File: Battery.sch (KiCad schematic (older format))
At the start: 21 parts, among them J3 USB_C_Receptacle_USB2.0, U4 SY6926

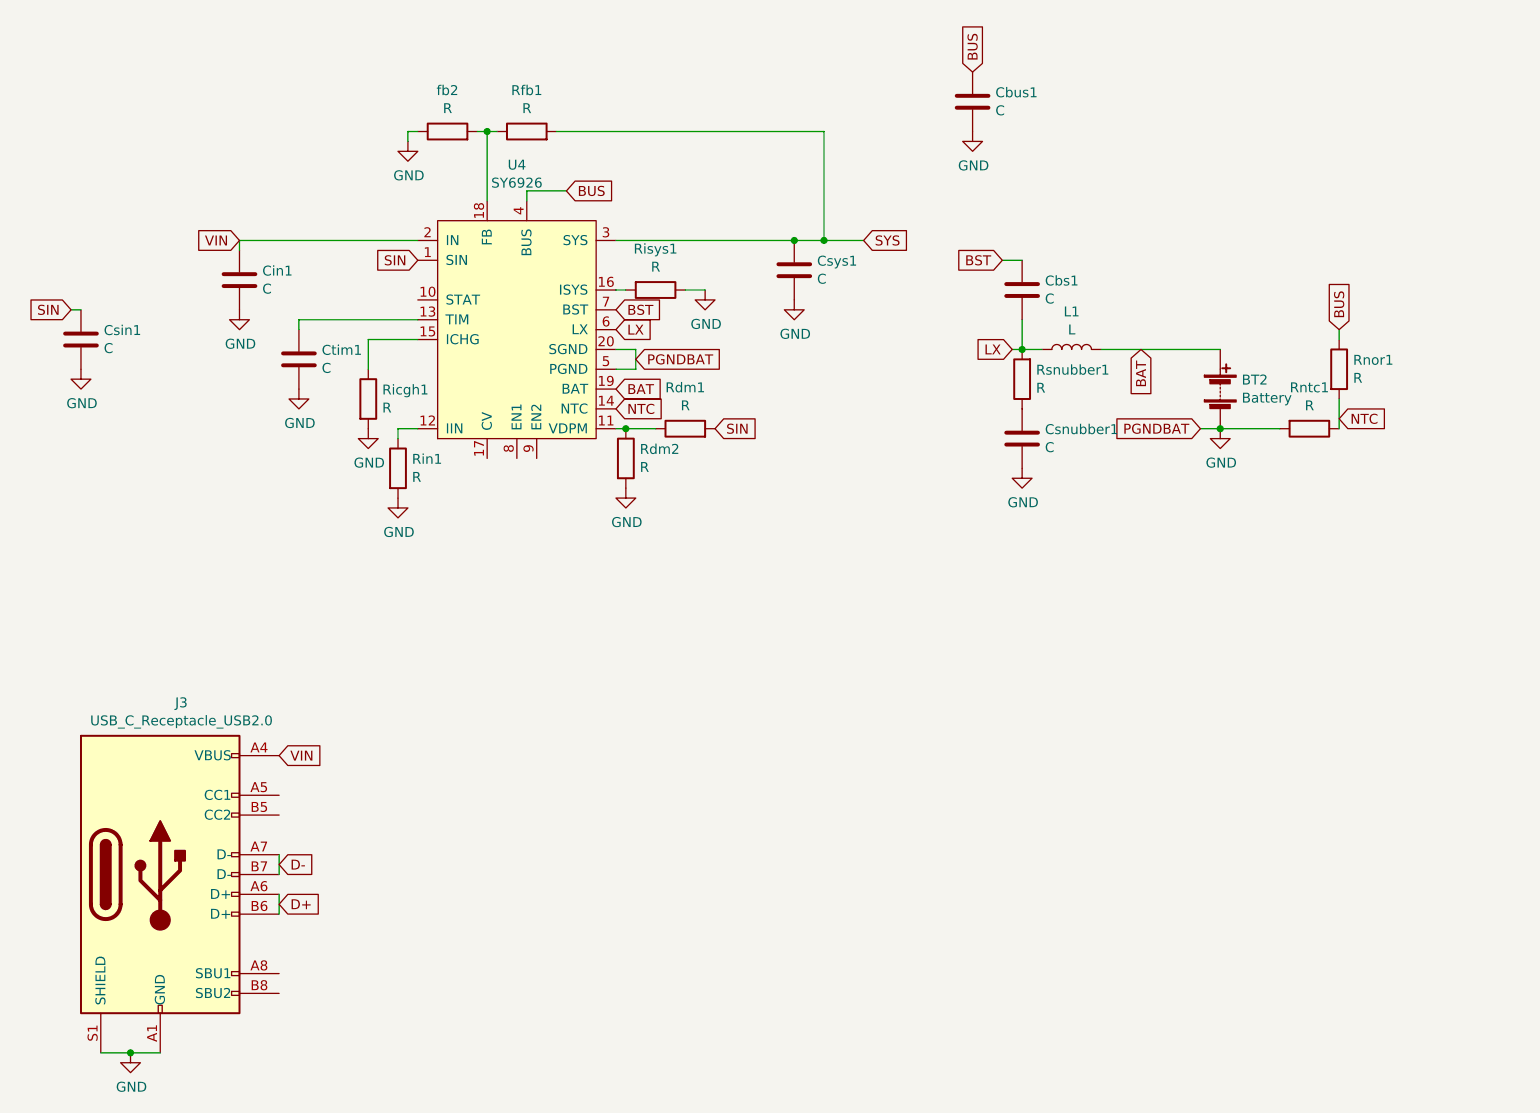
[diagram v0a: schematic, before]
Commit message: Added hardware battery disconnect
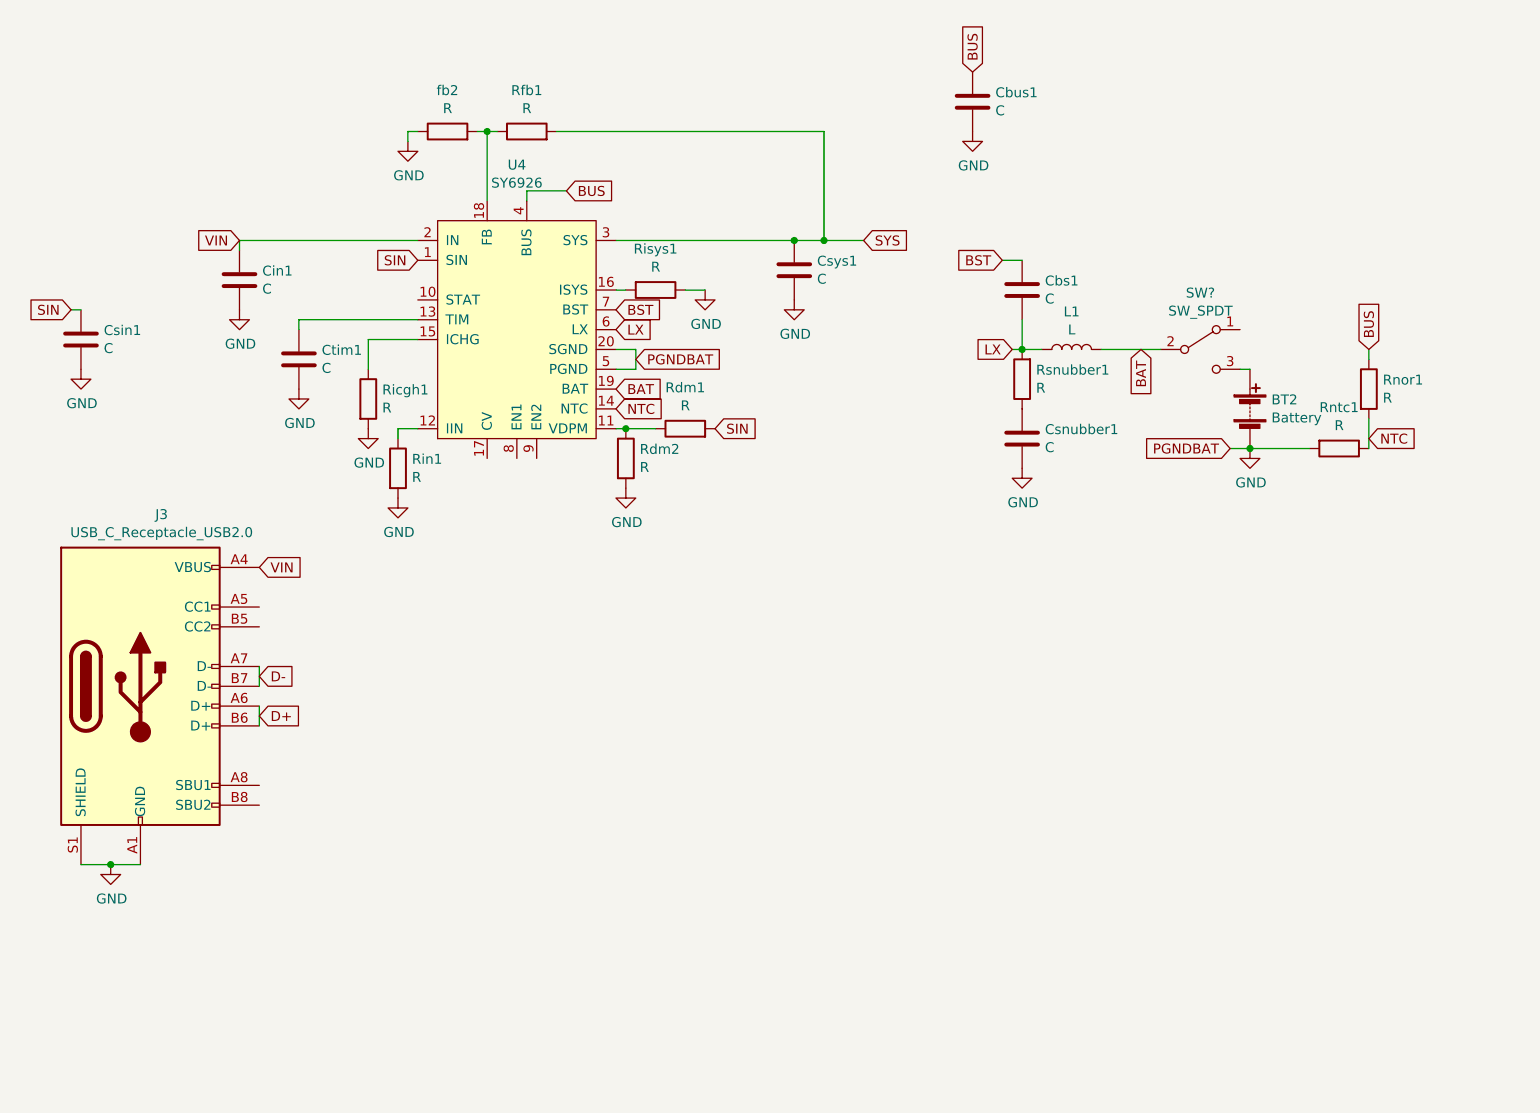
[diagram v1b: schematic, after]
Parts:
- added SW?: SW_SPDT, Hardware:SWINTCHFORBATTERY, symbol Switch:SW_SPDT
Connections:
- net BAT: now also SW?.2 (B); no longer BT2.1 (+)
- new net: BT2.1 (+), SW?.3 (C)
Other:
- moved on the sheet: BT2, J3, Rnor1, Rntc1
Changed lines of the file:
@@
 L Device:Battery BT2
 U 1 1 60BFF57C
-P 6650 2900
-F 0 "BT2" H 6758 2946 50  0000 L CNN
-F 1 "Battery" H 6758 2855 50  0000 L CNN
-F 2 "Connector_PinHeader_2.54mm:PinHeader_1x02_P2.54mm_Vertical" V 6650 2960 50  0001 C CNN
-F 3 "~" V 6650 2960 50  0001 C CNN
-	1    6650 2900
+P 6800 3000
+F 0 "BT2" H 6908 3046 50  0000 L CNN
+F 1 "Battery" H 6908 2955 50  0000 L CNN
+F 2 "Connector_PinHeader_2.54mm:PinHeader_1x02_P2.54mm_Vertical" V 6800 3060 50  0001 C CNN
+F 3 "~" V 6800 3060 50  0001 C CNN
+	1    6800 3000
 	1    0    0    -1
 $EndComp
@@
 $EndComp
 Wire Wire Line
-	6550 3100 6650 3100
+	6700 3200 6800 3200
 $Comp
 L power:GND #PWR028
 U 1 1 60C0B9D9
-P 6650 3100
-F 0 "#PWR028" H 6650 2850 50  0001 C CNN
-F 1 "GND" H 6655 2927 50  0000 C CNN
-F 2 "" H 6650 3100 50  0001 C CNN
-F 3 "" H 6650 3100 50  0001 C CNN
-	1    6650 3100
-	1    0    0    -1
-$EndComp
-Connection ~ 6650 3100
+P 6800 3200
+F 0 "#PWR028" H 6800 2950 50  0001 C CNN
+F 1 "GND" H 6805 3027 50  0000 C CNN
+F 2 "" H 6800 3200 50  0001 C CNN
+F 3 "" H 6800 3200 50  0001 C CNN
+	1    6800 3200
+	1    0    0    -1
+$EndComp
+Connection ~ 6800 3200
 Text GLabel 3350 1900 2    50   Input ~ 0
 BUS
-Text GLabel 7250 2600 1    50   Input ~ 0
+Text GLabel 7400 2700 1    50   Input ~ 0
 BUS
 $Comp
 L Device:R Rnor1
 U 1 1 60C0CFEE
-P 7250 2800
-F 0 "Rnor1" H 7320 2846 50  0000 L CNN
-F 1 "R" H 7320 2755 50  0000 L CNN
-F 2 "Resistor_SMD:R_0805_2012Metric" V 7180 2800 50  0001 C CNN
-F 3 "~" H 7250 2800 50  0001 C CNN
-	1    7250 2800
+P 7400 2900
+F 0 "Rnor1" H 7470 2946 50  0000 L CNN
+F 1 "R" H 7470 2855 50  0000 L CNN
+F 2 "Resistor_SMD:R_0805_2012Metric" V 7330 2900 50  0001 C CNN
+F 3 "~" H 7400 2900 50  0001 C CNN
+	1    7400 2900
 	1    0    0    -1
 $EndComp
@@
 L Device:R Rntc1
 U 1 1 60C0D8A7
-P 7100 3100
-F 0 "Rntc1" V 6893 3100 50  0000 C CNN
-F 1 "R" V 6984 3100 50  0000 C CNN
-F 2 "Resistor_SMD:R_0805_2012Metric" V 7030 3100 50  0001 C CNN
-F 3 "~" H 7100 3100 50  0001 C CNN
-	1    7100 3100
+P 7250 3200
+F 0 "Rntc1" V 7043 3200 50  0000 C CNN
+F 1 "R" V 7134 3200 50  0000 C CNN
+F 2 "Resistor_SMD:R_0805_2012Metric" V 7180 3200 50  0001 C CNN
+F 3 "~" H 7250 3200 50  0001 C CNN
+	1    7250 3200
 	0    1    1    0
 $EndComp
 Wire Wire Line
-	7250 3100 7250 2950
-Wire Wire Line
-	7250 2650 7250 2600
+	7400 3200 7400 3050
+Wire Wire Line
+	7400 2750 7400 2700
 $Comp
 L Device:L L1
@@
 Text GLabel 3700 2750 2    50   Input ~ 0
 PGNDBAT
-Wire Wire Line
-	6050 2700 6650 2700
 Text GLabel 3600 2500 2    50   Input ~ 0
 BST
@@
 Text GLabel 5600 2700 0    50   Input ~ 0
 LX
-Text GLabel 6550 3100 0    50   Input ~ 0
+Text GLabel 6700 3200 0    50   Input ~ 0
 PGNDBAT
 Wire Wire Line
@@
 Text GLabel 3600 3000 2    50   Input ~ 0
 NTC
-Text GLabel 7250 3050 2    50   Input ~ 0
+Text GLabel 7400 3150 2    50   Input ~ 0
 NTC
 Wire Wire Line
@@
 $EndComp
 Wire Wire Line
-	6650 3100 6950 3100
+	6800 3200 7100 3200
 Wire Wire Line
 	3350 1900 3150 1900
@@
 L Connector:USB_C_Receptacle_USB2.0 J3
 U 1 1 610152FB
-P 1300 5350
-F 0 "J3" H 1407 6217 50  0000 C CNN
-F 1 "USB_C_Receptacle_USB2.0" H 1407 6126 50  0000 C CNN
-F 2 "Connector_USB:USB_C_Receptacle_XKB_U262-16XN-4BVC11" H 1450 5350 50  0001 C CNN
-F 3 "https://www.usb.org/sites/default/files/documents/usb_type-c.zip" H 1450 5350 50  0001 C CNN
-	1    1300 5350
-	1    0    0    -1
-$EndComp
-Wire Wire Line
-	1300 6250 1150 6250
+P 1200 4400
+F 0 "J3" H 1307 5267 50  0000 C CNN
+F 1 "USB_C_Receptacle_USB2.0" H 1307 5176 50  0000 C CNN
+F 2 "Connector_USB:USB_C_Receptacle_XKB_U262-16XN-4BVC11" H 1350 4400 50  0001 C CNN
+F 3 "https://www.usb.org/sites/default/files/documents/usb_type-c.zip" H 1350 4400 50  0001 C CNN
+	1    1200 4400
+	1    0    0    -1
+$EndComp
+Wire Wire Line
+	1200 5300 1050 5300
 $Comp
 L power:GND #PWR053
 U 1 1 6101E2A9
-P 1150 6250
-F 0 "#PWR053" H 1150 6000 50  0001 C CNN
-F 1 "GND" H 1155 6077 50  0000 C CNN
-F 2 "" H 1150 6250 50  0001 C CNN
-F 3 "" H 1150 6250 50  0001 C CNN
-	1    1150 6250
-	1    0    0    -1
-$EndComp
-Connection ~ 1150 6250
-Wire Wire Line
-	1150 6250 1000 6250
+P 1050 5300
+F 0 "#PWR053" H 1050 5050 50  0001 C CNN
+F 1 "GND" H 1055 5127 50  0000 C CNN
+F 2 "" H 1050 5300 50  0001 C CNN
+F 3 "" H 1050 5300 50  0001 C CNN
+	1    1050 5300
+	1    0    0    -1
+$EndComp
+Connection ~ 1050 5300
+Wire Wire Line
+	1050 5300 900  5300
 Text GLabel 1700 2150 0    50   Input ~ 0
 VIN
-Text GLabel 1900 4750 2    50   Input ~ 0
+Text GLabel 1800 3800 2    50   Input ~ 0
 VIN
 Wire Wire Line
-	1900 5250 1900 5350
-Wire Wire Line
-	1900 5450 1900 5550
-Text GLabel 1900 5300 2    50   Input ~ 0
+	1800 4300 1800 4400
+Wire Wire Line
+	1800 4500 1800 4600
+Text GLabel 1800 4350 2    50   Input ~ 0
 D-
-Text GLabel 1900 5500 2    50   Input ~ 0
+Text GLabel 1800 4550 2    50   Input ~ 0
 D+
+Wire Wire Line
+	6800 2800 6750 2800
+Wire Wire Line
+	6050 2700 6350 2700
+$Comp
+L Switch:SW_SPDT SW?
+U 1 1 60A4FBE3
+P 6550 2700
+F 0 "SW?" H 6550 2985 50  0000 C CNN
+F 1 "SW_SPDT" H 6550 2894 50  0000 C CNN
+F 2 "Hardware:SWINTCHFORBATTERY" H 6550 2700 50  0001 C CNN
+F 3 "~" H 6550 2700 50  0001 C CNN
+	1    6550 2700
+	1    0    0    -1
+$EndComp
 $EndSCHEMATC

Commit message: Ja crap toch weer aan de PCB gezeten
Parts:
- gave numbers to parts that had none: 1
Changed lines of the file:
@@
 	6050 2700 6350 2700
 $Comp
-L Switch:SW_SPDT SW?
+L Switch:SW_SPDT SW2
 U 1 1 60A4FBE3
 P 6550 2700
-F 0 "SW?" H 6550 2985 50  0000 C CNN
+F 0 "SW2" H 6550 2985 50  0000 C CNN
 F 1 "SW_SPDT" H 6550 2894 50  0000 C CNN
 F 2 "Hardware:SWINTCHFORBATTERY" H 6550 2700 50  0001 C CNN

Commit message: Added SY6926 component values and some minor cleanup
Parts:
- Cin1: value C -> 20uF
- L1: value L -> 1.65uH
- Rdm1, Rfb1: value R -> 33K
- Rdm2: value R -> 9.1K
- Ricgh1: value R -> 10.666K
- Rin1: value R -> 1K
- Risys1: value R -> 36K
- fb2: value R -> 10.3K
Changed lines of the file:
@@
 P 3650 3250
 F 0 "Rdm2" H 3720 3296 50  0000 L CNN
-F 1 "R" H 3720 3205 50  0000 L CNN
+F 1 "9.1K" H 3720 3205 50  0000 L CNN
 F 2 "Resistor_SMD:R_0805_2012Metric" V 3580 3250 50  0001 C CNN
 F 3 "~" H 3650 3250 50  0001 C CNN
@@
 P 3950 3100
 F 0 "Rdm1" V 4157 3100 50  0000 C CNN
-F 1 "R" V 4066 3100 50  0000 C CNN
+F 1 "33K" V 4066 3100 50  0000 C CNN
 F 2 "Resistor_SMD:R_0805_2012Metric" V 3880 3100 50  0001 C CNN
 F 3 "~" H 3950 3100 50  0001 C CNN
@@
 P 2500 3300
 F 0 "Rin1" H 2570 3346 50  0000 L CNN
-F 1 "R" H 2570 3255 50  0000 L CNN
+F 1 "1K" H 2570 3255 50  0000 L CNN
 F 2 "Resistor_SMD:R_0805_2012Metric" V 2430 3300 50  0001 C CNN
 F 3 "~" H 2500 3300 50  0001 C CNN
@@
 P 2350 2950
 F 0 "Ricgh1" H 2420 2996 50  0000 L CNN
-F 1 "R" H 2420 2905 50  0000 L CNN
+F 1 "10.666K" H 2420 2905 50  0000 L CNN
 F 2 "Resistor_SMD:R_0805_2012Metric" V 2280 2950 50  0001 C CNN
 F 3 "~" H 2350 2950 50  0001 C CNN
@@
 P 1700 2350
 F 0 "Cin1" H 1815 2396 50  0000 L CNN
-F 1 "C" H 1815 2305 50  0000 L CNN
+F 1 "20uF" H 1815 2305 50  0000 L CNN
 F 2 "Capacitor_SMD:C_0805_2012Metric" H 1738 2200 50  0001 C CNN
 F 3 "~" H 1700 2350 50  0001 C CNN
@@
 P 5900 2700
 F 0 "L1" V 6090 2700 50  0000 C CNN
-F 1 "L" V 5999 2700 50  0000 C CNN
+F 1 "1.65uH" V 5999 2700 50  0000 C CNN
 F 2 "Connector_PinHeader_2.54mm:PinHeader_1x02_P2.54mm_Vertical" H 5900 2700 50  0001 C CNN
 F 3 "~" H 5900 2700 50  0001 C CNN
@@
 P 3800 2400
 F 0 "Risys1" V 3593 2400 50  0000 C CNN
-F 1 "R" V 3684 2400 50  0000 C CNN
+F 1 "36K" V 3684 2400 50  0000 C CNN
 F 2 "Resistor_SMD:R_0805_2012Metric" V 3730 2400 50  0001 C CNN
 F 3 "~" H 3800 2400 50  0001 C CNN
@@
 P 2750 1600
 F 0 "fb2" V 2957 1600 50  0000 C CNN
-F 1 "R" V 2866 1600 50  0000 C CNN
+F 1 "10.3K" V 2866 1600 50  0000 C CNN
 F 2 "Resistor_SMD:R_0805_2012Metric" V 2680 1600 50  0001 C CNN
 F 3 "~" H 2750 1600 50  0001 C CNN
@@
 P 3150 1600
 F 0 "Rfb1" V 3357 1600 50  0000 C CNN
-F 1 "R" V 3266 1600 50  0000 C CNN
+F 1 "33K" V 3266 1600 50  0000 C CNN
 F 2 "Resistor_SMD:R_0805_2012Metric" V 3080 1600 50  0001 C CNN
 F 3 "~" H 3150 1600 50  0001 C CNN

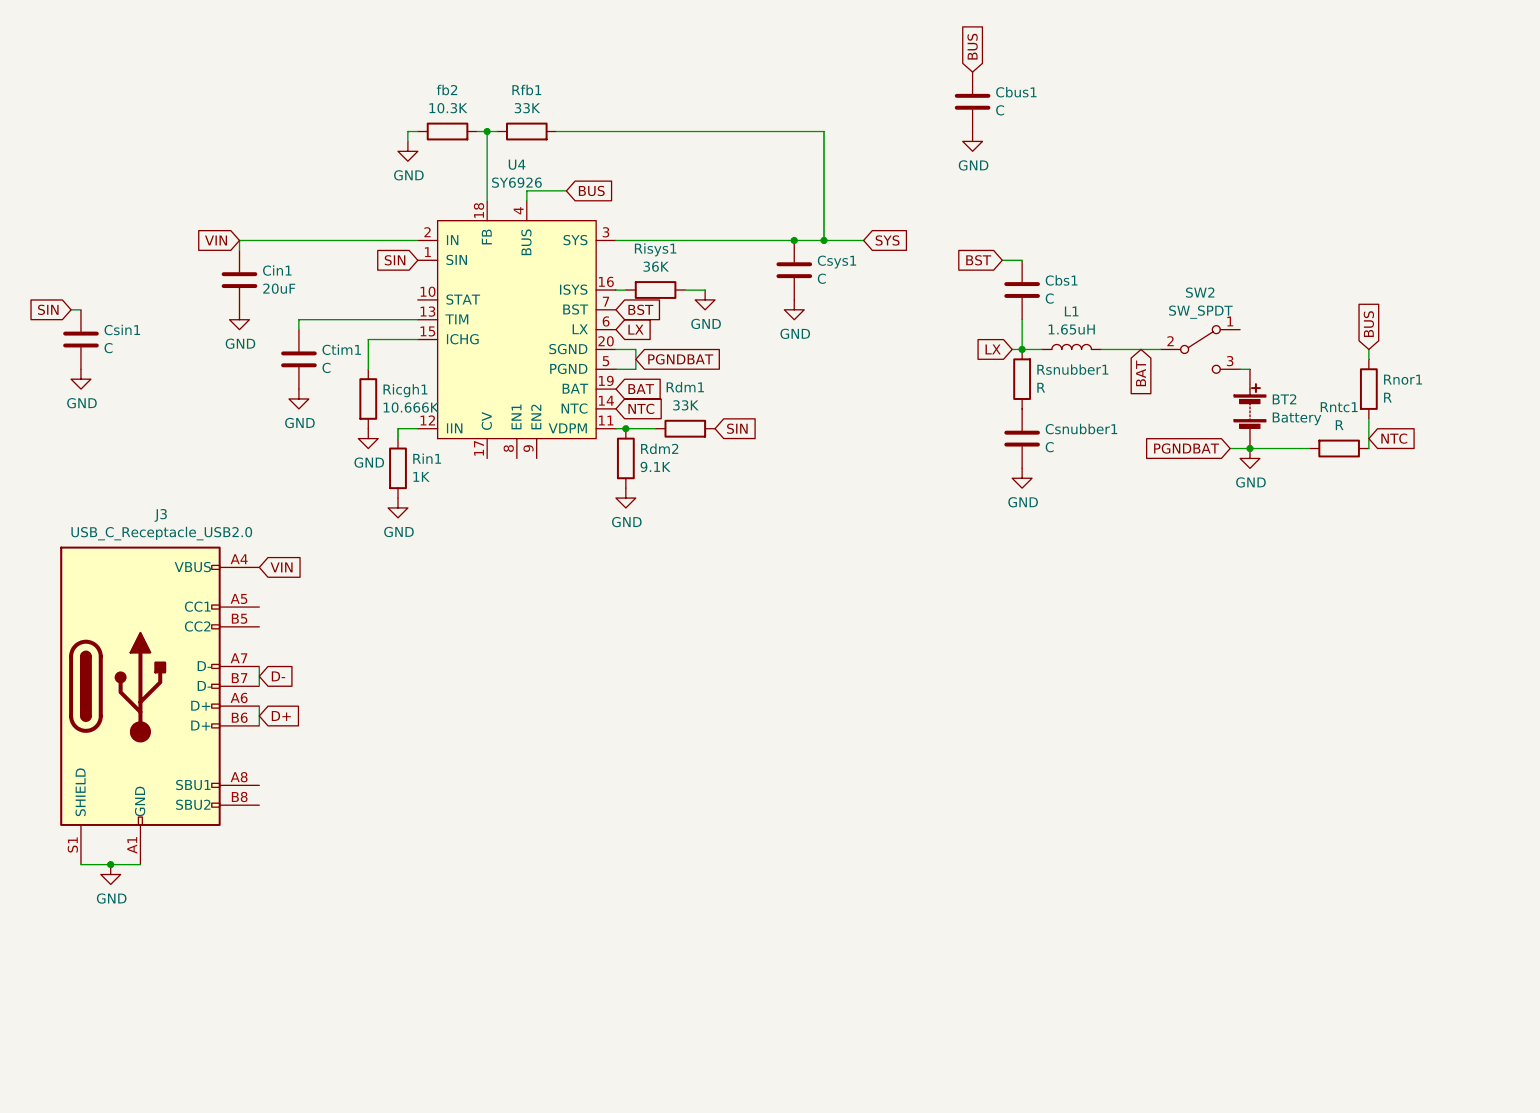
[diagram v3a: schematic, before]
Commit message: NTC circuit and values added
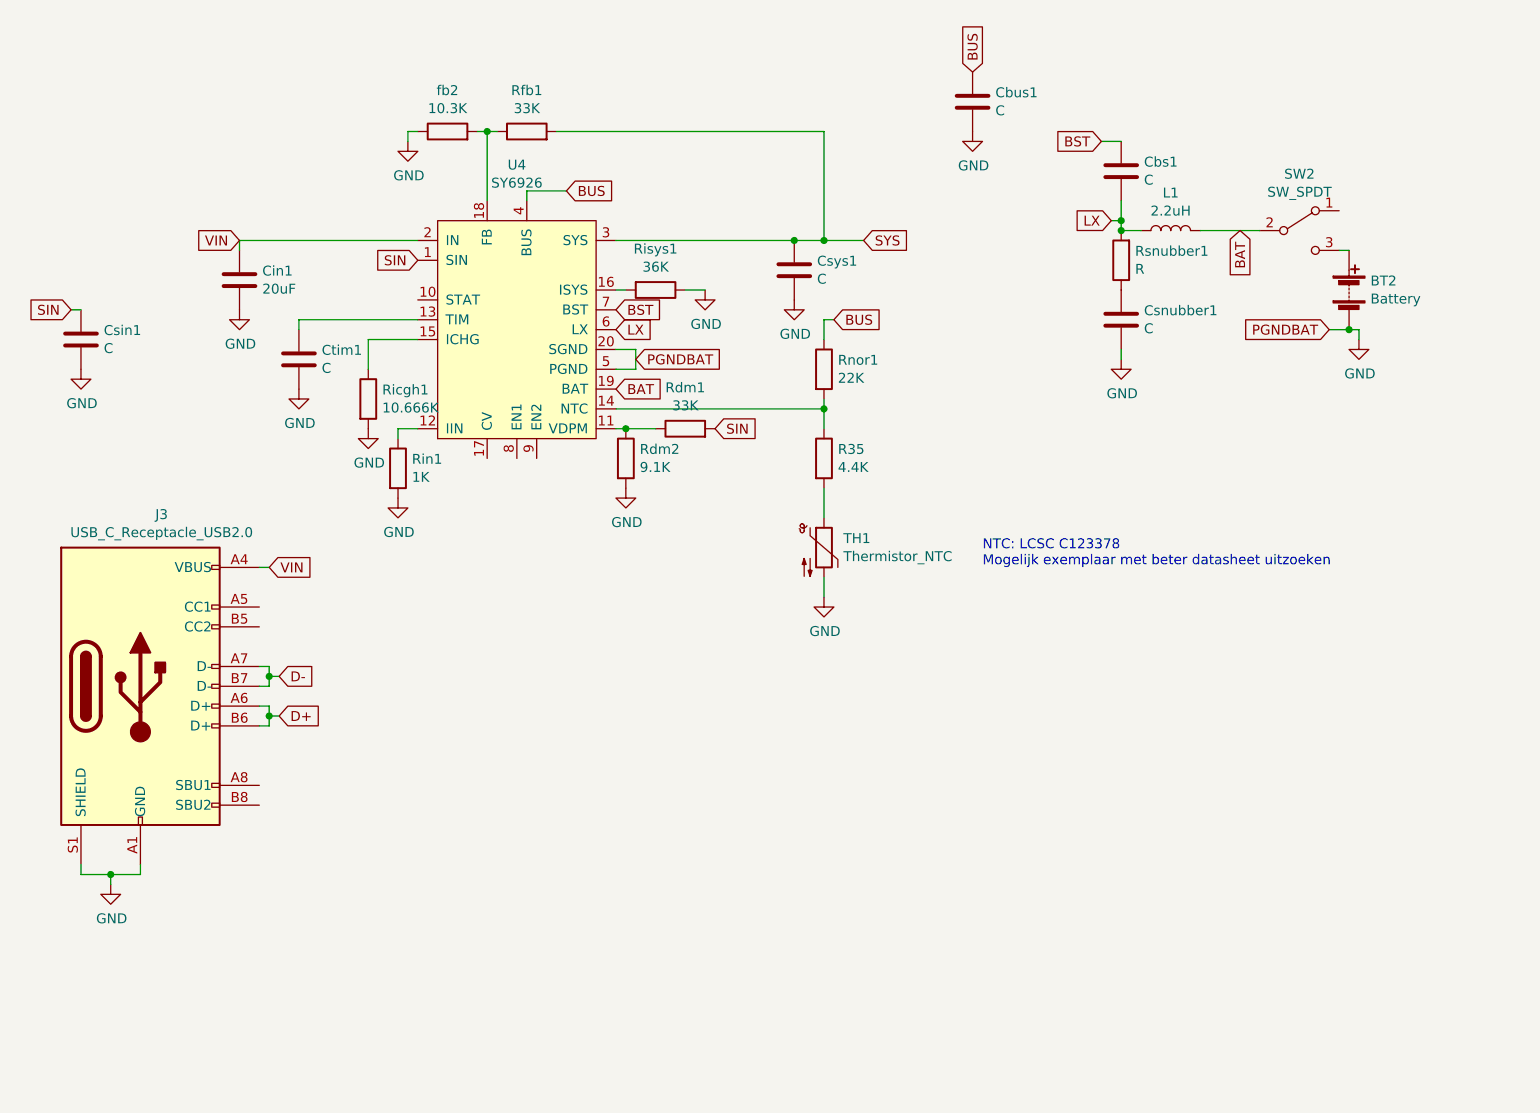
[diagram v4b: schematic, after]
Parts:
- removed Rntc1: R, Resistor_SMD:R_0805_2012Metric, symbol Device:R
- added R35: 4.4K, symbol Device:R
- added TH1: Thermistor_NTC, symbol Device:Thermistor_NTC
- L1: value 1.65uH -> 2.2uH
- Rnor1: value R -> 22K
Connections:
- net GND: now also TH1.2
- net NTC: no longer names the net of Rnor1.2, U4.14 (NTC)
- net NTC: now also R35.1
- new net: R35.2, TH1.1
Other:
- note added: "NTC: LCSC C123378\nMogelijk exemplaar met beter datasheet uitzoeken"
- moved on the sheet: BT2, Cbs1, Csnubber1, L1, Rnor1, Rsnubber1, SW2
